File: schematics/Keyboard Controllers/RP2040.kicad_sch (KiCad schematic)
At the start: 12 parts, among them J2 Conn_ARM_SWD_TagConnect_TC203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, J3 USB_C_Receptacle, U9 ECMF02-2AMX6

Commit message: Refactor RP2040, change to oscillator over crystal
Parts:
- removed C44, C45: 100nF, Capacitor_SMD:C_0402_1005Metric, symbol Device:C_Small
- removed C46: 10uF, Capacitor_SMD:C_0805_2012Metric, symbol Device:C_Small
- removed FB3, FB4: BLM15PX330SN1D, Inductor_SMD:L_0402_1005Metric, symbol Device:FerriteBead_Small
- removed J3: USB_C_Receptacle, Connector_USB:USB_C_Receptacle_GCT_USB4105-xx-A_16P_TopMnt_Horizontal, symbol Connector:USB_C_Receptacle_USB2.0_16P
- removed R21, R22: 5K1, Resistor_SMD:R_0402_1005Metric, symbol Device:R_Small
- removed U9: ECMF02-2AMX6, Package_DFN_QFN:ST_UQFN-6L_1.5x1.7mm_P0.5mm, symbol Power_Protection:ECMF02-2AMX6
- added C4, C5: 10uF, Capacitor_SMD:C_0805_2012Metric, symbol Device:C_Small
- added D1: SK6812_MINI_E, Mad_Footprints:WS2812C-2020, symbol Mad_Symbols:WS2812
- added D2: LED, LED_SMD:LED_0603_1608Metric, symbol Device:LED
- added R5: 2K2, Resistor_SMD:R_0402_1005Metric, symbol Device:R
- added U3: NCP1117-3.3_SOT223, Package_TO_SOT_SMD:SOT-223-3_TabPin2, symbol Regulator_Linear:NCP1117-3.3_SOT223
- R3: renamed from R7; MPN (none) -> RC0402FR-072K2L; Manufacturer UNI-ROYAL(Uniroyal Elec) -> YAGEO; Price (none) -> $0.16; Rating (none) -> RES 2.2K OHM 1% 1/16W 0402; Supplier (none) -> Digikey; Supplier PN (none) -> 311-2.20KLRCT-ND
- renumbered R8 to R4
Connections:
- net 3V3: now also C5.1, D1.4 (VDD), R5.1, U3.2 (VO)
- net GND: now also C4.2, C5.2, D1.2 (GND), D2.1 (K), U3.1 (GND)
- net STATUS_LED_DO: now also D1.3 (DIN)
- new net: D2.2 (A), R5.2
- new net 5V: C4.1, U3.3 (VI)
- no-connect marks 14 -> 5
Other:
- sheet RP2040 ports: added 3V3, SWCLK, SWDIO, ~{RST}; removed 5V
- note added: "3V3 Reg"
- note added: "Power LED"
- note added: "Status LED"
- note removed: "EMCZ0"
- note removed: "EMCZ1"
- moved on the sheet: R3, R4

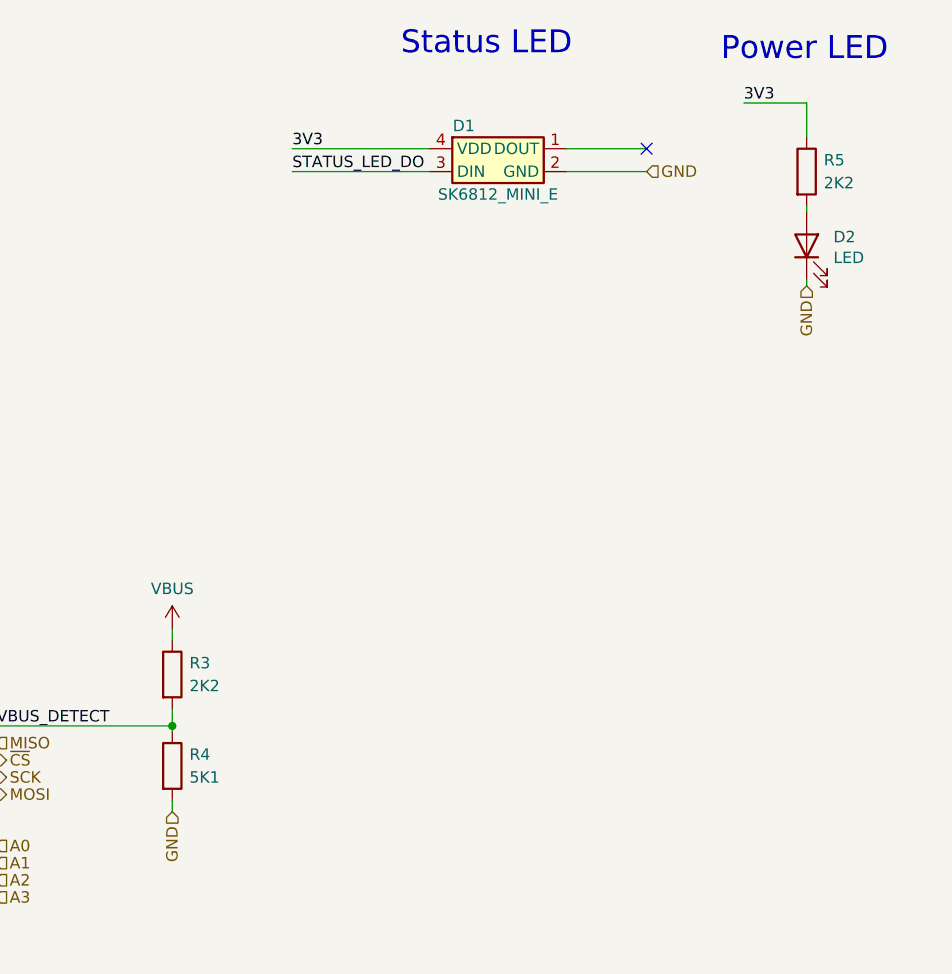
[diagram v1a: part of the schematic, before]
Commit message: Cleanup, BOM Update, Expose LED DOUT for internal status led
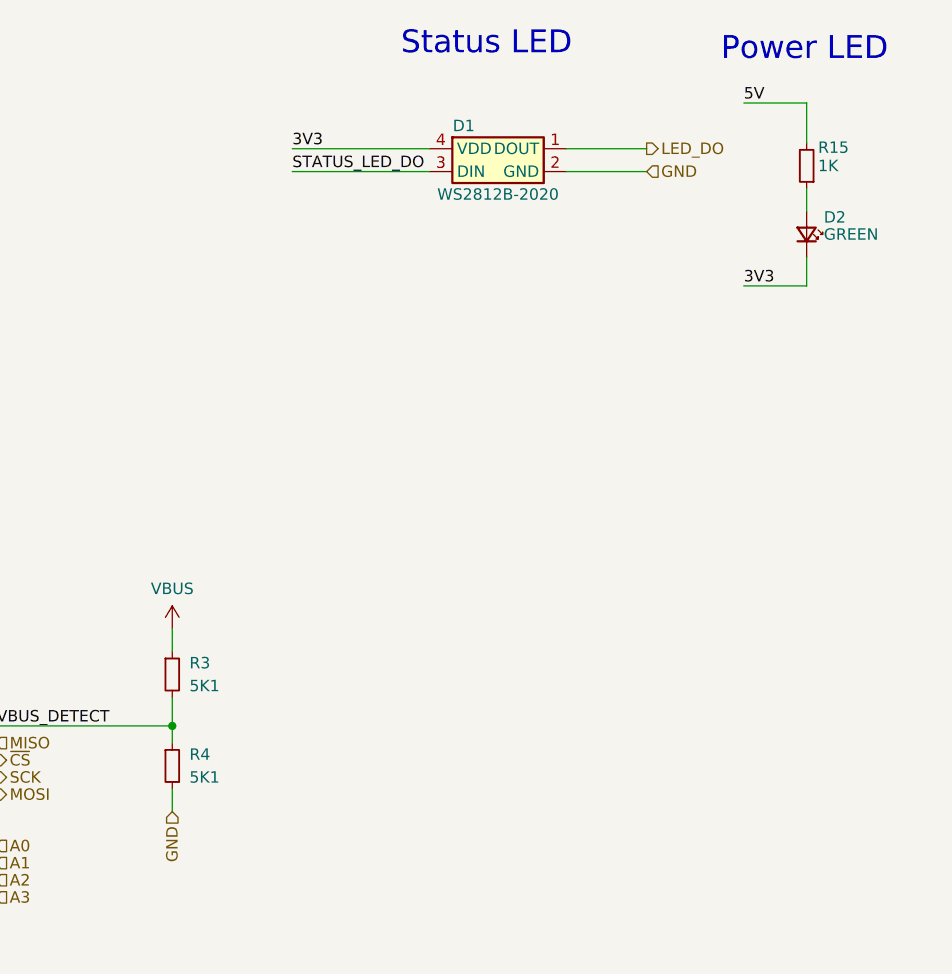
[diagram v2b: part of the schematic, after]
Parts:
- removed R3, R5: 2K2, Resistor_SMD:R_0402_1005Metric, symbol Device:R
- added R15: 1K, Resistor_SMD:R_0402_1005Metric, symbol Device:R_Small
- added R3: 5K1, Resistor_SMD:R_0402_1005Metric, symbol Device:R_Small
- D1: value SK6812_MINI_E -> WS2812B-2020; JLC Basic N -> (none); LCSC C965556 -> (none); MPN WS2812C-2020 -> WS2812B-2020; Price $0.42 -> $ 0.36; Substitute N -> (none); Supplier PN C965556 -> C965555
- D2: value LED -> GREEN; symbol Device:LED -> Device:LED_Small; JLC Basic Y -> (none); LCSC C268294 -> (none); MPN (none) -> 150060VS75000; MPN  OSK40603C1E -> (none); Manufacturer OptoSupply -> Würth Elektronik; Price (none) -> $0.24; Rating (none) -> LED GREEN CLEAR 0603 SMD; Substitute Y - any pink -> (none); Supplier (none) -> Digikey; Supplier PN (none) -> 732-4980-1-ND
- R4: symbol Device:R -> Device:R_Small
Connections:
- net 3V3: now also D2.1 (K)
- net 5V: now also R15.2
- net GND: no longer D2.1 (K)
- net VBUS: now also R3.1
- net VBUS_DETECT: now also R3.2
- net at D2.2 (A): now also R15.1
- net LED_DO: now reaches D1.1 (DOUT)
- no-connect marks 5 -> 4
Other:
- moved on the sheet: D2
